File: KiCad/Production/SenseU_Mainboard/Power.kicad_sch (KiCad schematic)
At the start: 16 parts, among them Q2 AO3421E, U3 AP2112K-3.3TRG1

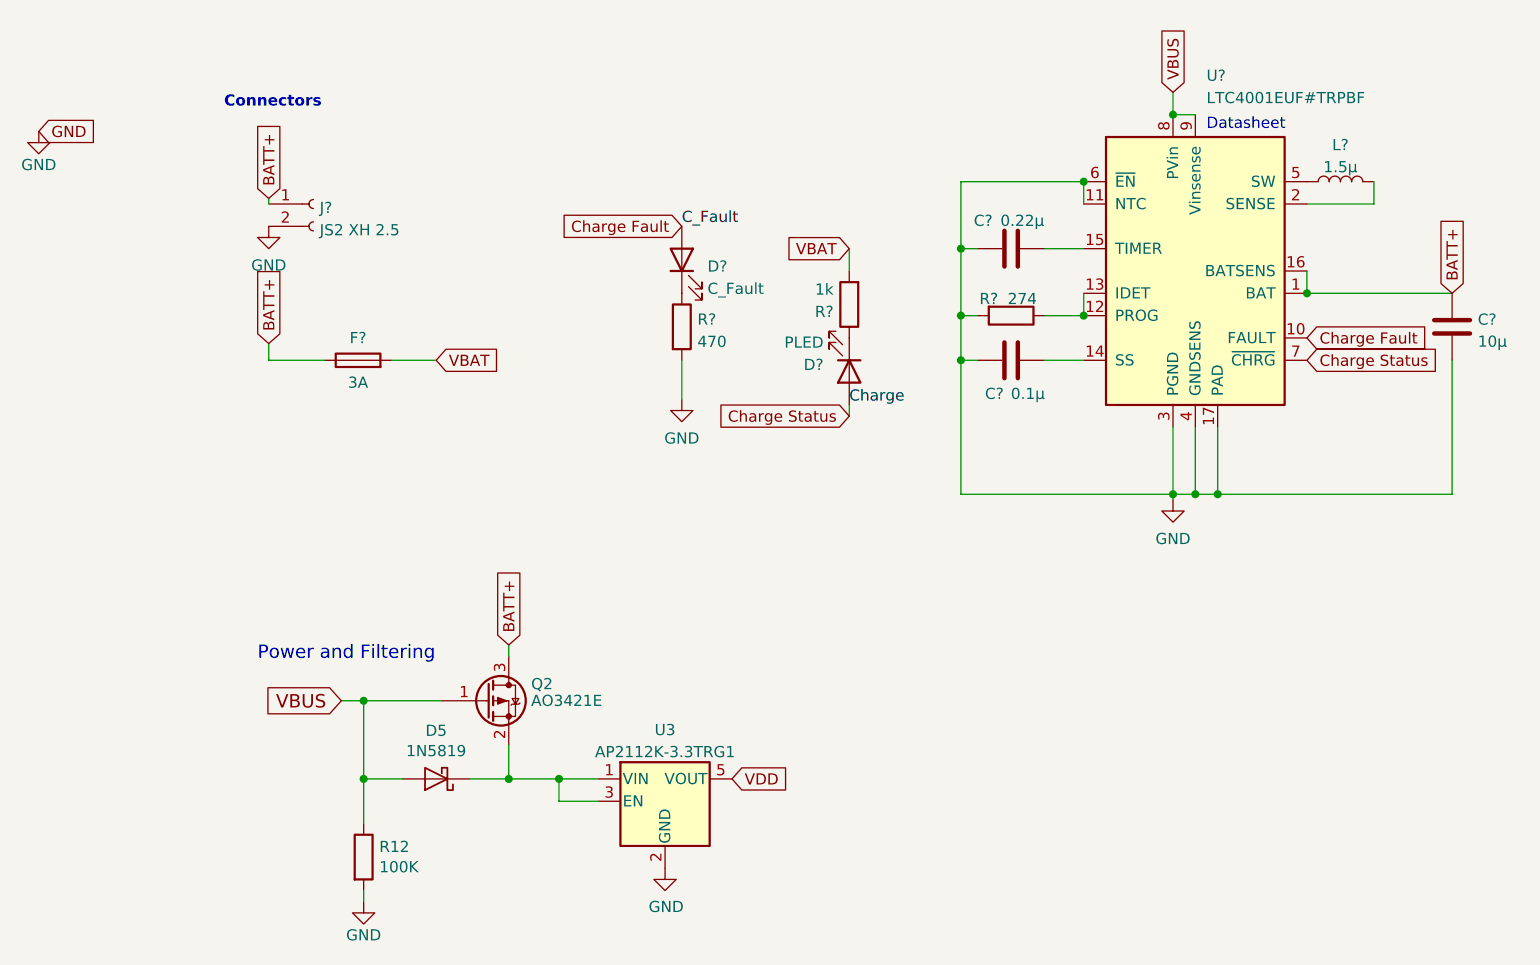
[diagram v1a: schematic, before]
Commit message: removed batt co to fpga and added switch
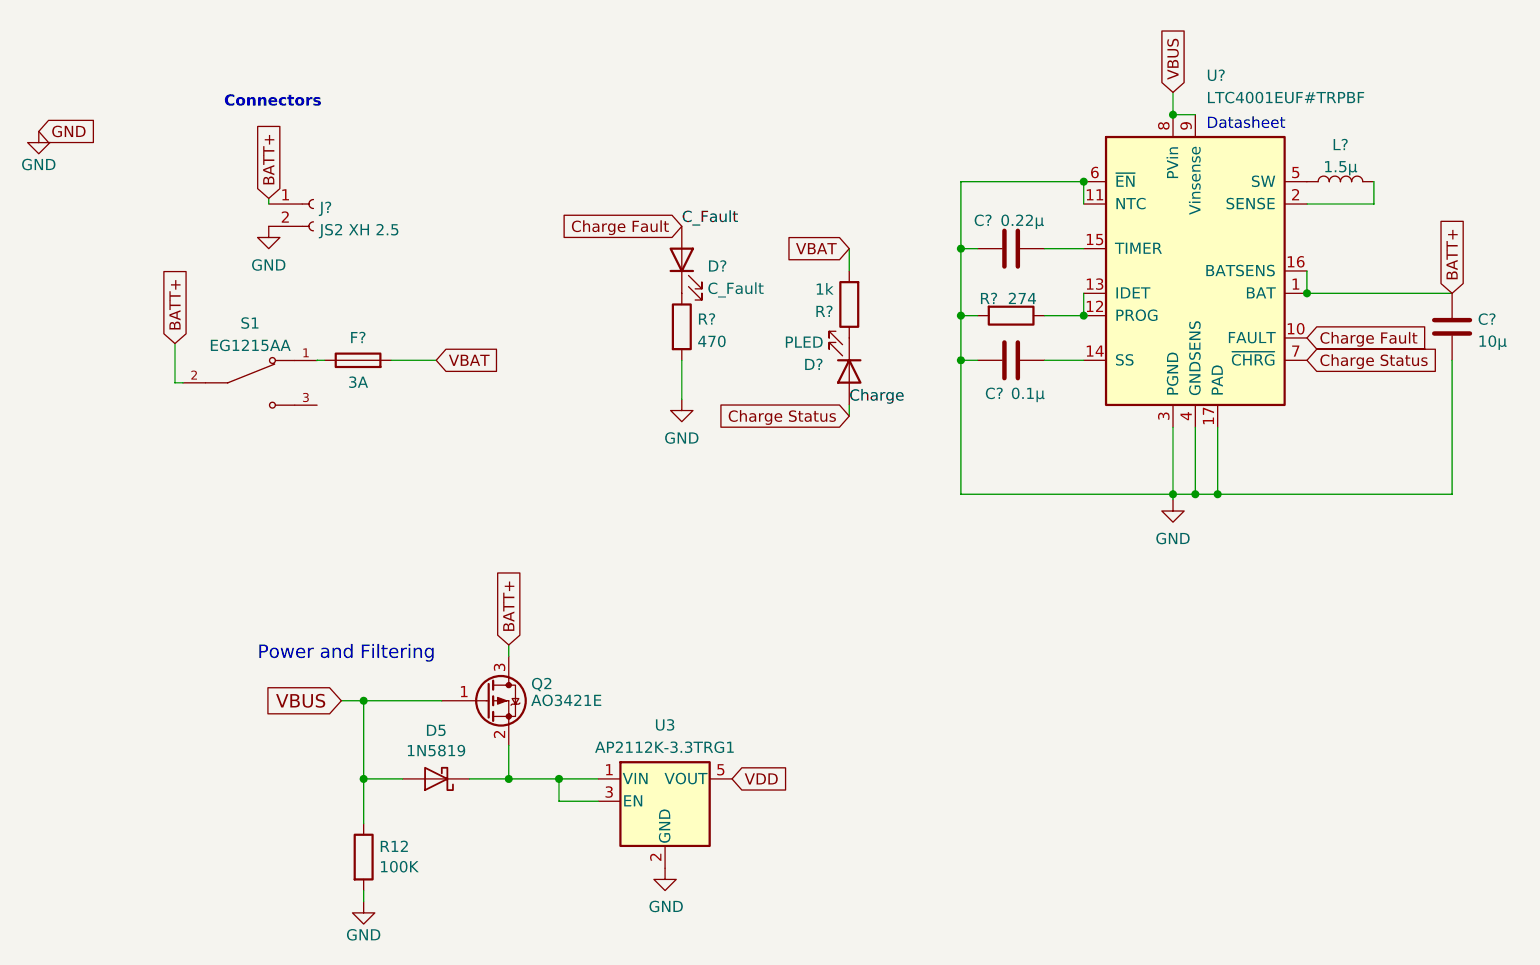
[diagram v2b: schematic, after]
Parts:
- added S1: EG1215AA, SW_EG1215AA, symbol switch:EG1215AA
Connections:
- net BATT+: now also S1.2; no longer F?.1
- new net: F?.1, S1.1
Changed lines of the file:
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@@
+    (stroke (width 0) (type default))
+  )
+  (wire (pts (xy 69.5074 80.4147) (xy 68.58 80.4147))
     (stroke (width 0) (type default))
   )
@@
     (stroke (width 0) (type default))
   )
-  (wire (pts (xy 79.248 77.851) (xy 85.598 77.851))
-    (stroke (width 0) (type default))
-  )
   (wire (pts (xy 182.118 93.726) (xy 182.118 93.091))
     (stroke (width 0) (type default))
@@
     (stroke (width 0) (type default))
   )
-  (wire (pts (xy 79.248 75.946) (xy 79.248 77.851))
+  (wire (pts (xy 68.58 75.946) (xy 68.58 80.4147))
     (stroke (width 0) (type default))
   )
@@
     (stroke (width 0) (type default))
   )
+  (wire (pts (xy 85.598 77.851) (xy 84.7474 77.851))
+    (stroke (width 0) (type default))
+  )
   (wire (pts (xy 204.978 60.071) (xy 204.978 57.531))
     (stroke (width 0) (type default))
@@
   )
   (wire (pts (xy 106.553 125.476) (xy 112.268 125.476))
+    (stroke (width 0) (type default))
+  )
+  (wire (pts (xy 84.7474 77.851) (xy 84.7474 77.8747))
     (stroke (width 0) (type default))
   )
@@
     (effects (font (size 1.27 1.27)) (justify left bottom))
   )
-  (global_label "BATT+" (shape input) (at 79.248 75.946 90) (fields_autoplaced)
+  (global_label "BATT+" (shape input) (at 68.58 75.946 90) (fields_autoplaced)
     (effects (font (size 1.27 1.27)) (justify left))
-    (property "Intersheetrefs" "${INTERSHEET_REFS}" (at 79.248 68.0341 90)
+    (property "Intersheetrefs" "${INTERSHEET_REFS}" (at 68.58 68.0341 90)
       (effects (font (size 1.27 1.27)) (justify left) hide)
     )
@@
   (symbol (lib_id "Regulator_Linear:AP2112K-3.3") (at 124.333 128.016 0) (unit 1)
     (in_bom yes) (on_board yes) (dnp no) (fields_autoplaced)
-    (property "Reference" "U3" (at 124.333 119.9068 0)
-      (effects (font (size 1.27 1.27)))
-    )
-    (property "Value" "AP2112K-3.3TRG1\n" (at 124.333 122.412 0)
+    (property "Reference" "U3" (at 124.333 119.38 0)
+      (effects (font (size 1.27 1.27)))
+    )
+    (property "Value" "AP2112K-3.3TRG1\n" (at 124.333 121.92 0)
       (effects (font (size 1.27 1.27)))
     )
@@
         )
       )
+    )
+  )
+  (symbol (lib_id "switch:EG1215AA") (at 77.1274 80.4147 0) (unit 1)
+    (in_bom yes) (on_board yes) (dnp no) (fields_autoplaced)
+    (property "Reference" "S1" (at 77.1274 73.66 0)
+      (effects (font (size 1.27 1.27)))
+    )
+    (property "Value" "EG1215AA" (at 77.1274 76.2 0)
+      (effects (font (size 1.27 1.27)))
+    )
+    (property "Footprint" "SW_EG1215AA" (at 77.1274 80.4147 0)
+      (effects (font (size 1.27 1.27)) (justify bottom) hide)
+    )
+    (property "Datasheet" "" (at 77.1274 80.4147 0)
+      (effects (font (size 1.27 1.27)) hide)
+    )
+    (property "PARTREV" "A" (at 77.1274 80.4147 0)
+      (effects (font (size 1.27 1.27)) (justify bottom) hide)
+    )
+    (property "STANDARD" "Manufacturer Recommendations" (at 77.1274 80.4147 0)
+      (effects (font (size 1.27 1.27)) (justify bottom) hide)
+    )
+    (property "MAXIMUM_PACKAGE_HEIGHT" "1.40mm" (at 77.1274 80.4147 0)
+      (effects (font (size 1.27 1.27)) (justify bottom) hide)
+    )
+    (property "MANUFACTURER" "E Switch" (at 77.1274 80.4147 0)
+      (effects (font (size 1.27 1.27)) (justify bottom) hide)
+    )
+    (pin "1")
+    (pin "2")
+    (pin "3")
+    (instances
+      (project "SenseU_Mainboard"
+        (path "/43872b54-cf9c-4c7b-870d-631baccef0c0/19a6c197-7c63-4043-b240-1314a2f063a4"
+          (reference "S1") (unit 1)
+        )
+      )

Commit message: routing SenseU done
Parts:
- C? (x3): footprint Capacitor_SMD:C_0603_1608Metric_Pad1.08x0.95mm_HandSolder -> Capacitor_SMD:C_0603_1608Metric
- S1: footprint SW_EG1215AA -> switch:SW_EG1215AA
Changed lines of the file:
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@@
       (effects (font (size 1.27 1.27)))
     )
-    (property "Footprint" "Capacitor_SMD:C_0603_1608Metric_Pad1.08x0.95mm_HandSolder" (at 167.513 64.1858 0)
+    (property "Footprint" "Capacitor_SMD:C_0603_1608Metric" (at 167.513 64.1858 0)
       (effects (font (size 1.27 1.27)) hide)
     )
@@
       (effects (font (size 1.27 1.27)) (justify left))
     )
-    (property "Footprint" "Capacitor_SMD:C_0603_1608Metric_Pad1.08x0.95mm_HandSolder" (at 214.8332 77.851 0)
+    (property "Footprint" "Capacitor_SMD:C_0603_1608Metric" (at 214.8332 77.851 0)
       (effects (font (size 1.27 1.27)) hide)
     )
@@
       (effects (font (size 1.27 1.27)))
     )
-    (property "Footprint" "Capacitor_SMD:C_0603_1608Metric_Pad1.08x0.95mm_HandSolder" (at 167.513 76.8858 0)
+    (property "Footprint" "Capacitor_SMD:C_0603_1608Metric" (at 167.513 76.8858 0)
       (effects (font (size 1.27 1.27)) hide)
     )
@@
       (effects (font (size 1.27 1.27)))
     )
-    (property "Footprint" "SW_EG1215AA" (at 77.1274 80.4147 0)
+    (property "Footprint" "switch:SW_EG1215AA" (at 77.1274 80.4147 0)
       (effects (font (size 1.27 1.27)) (justify bottom) hide)
     )
